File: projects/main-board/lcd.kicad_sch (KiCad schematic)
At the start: 10 parts

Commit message: Add footprints and 3D models
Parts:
- removed J1: ~, symbol symbol-library:NHD-4.3-480272EF-ASXP
- added J5: NHD-4.3-480272EF-ASXP (Molex 54104-4031), footprint-library:Molex 54104-4031, symbol symbol-library:NHD-4.3-480272EF-ASXP
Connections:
- net 3V3: now also J5.4 (VDD)
- net BACKLIGHT_N: now also J5.1 (LED-)
- net BACKLIGHT_P: now also J5.2 (LED+)
- net GND: now also J5.29 (GND), J5.3 (GND), J5.36 (GND)
- net LCD.B0: now also J5.21 (B0)
- net LCD.B1: now also J5.22 (B1)
- net LCD.B2: now also J5.23 (B2)
- net LCD.B3: now also J5.24 (B3)
- net LCD.B4: now also J5.25 (B4)
- net LCD.B5: now also J5.26 (B5)
- net LCD.B6: now also J5.27 (B6)
- net LCD.B7: now also J5.28 (B7)
- net LCD.CLK: now also J5.30 (CLKIN)
- net LCD.DE: now also J5.34 (DEN)
- net LCD.EN: now also J5.31 (STBYB)
- net LCD.G0: now also J5.13 (G0)
- net LCD.G1: now also J5.14 (G1)
- net LCD.G2: now also J5.15 (G2)
- net LCD.G3: now also J5.16 (G3)
- net LCD.G4: now also J5.17 (G4)
- net LCD.G5: now also J5.18 (G5)
- net LCD.G6: now also J5.19 (G6)
- net LCD.G7: now also J5.20 (G7)
- net LCD.HSYNC: now also J5.32 (HSD)
- net LCD.R0: now also J5.5 (R0)
- net LCD.R1: now also J5.6 (R1)
- net LCD.R2: now also J5.7 (R2)
- net LCD.R3: now also J5.8 (R3)
- net LCD.R4: now also J5.9 (R4)
- net LCD.R5: now also J5.10 (R5)
- net LCD.R6: now also J5.11 (R6)
- net LCD.R7: now also J5.12 (R7)
- net LCD.VSYNC: now also J5.33 (VSD)
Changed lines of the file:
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@@
-	)
-	(symbol
-		(lib_id "symbol-library:NHD-4.3-480272EF-ASXP")
-		(at 223.52 39.37 0)
-		(unit 1)
-		(exclude_from_sim no)
-		(in_bom yes)
-		(on_board yes)
-		(dnp no)
-		(property "Reference" "J1"
-			(at 224.536 38.1 0)
-			(effects
-				(font
-					(size 1.27 1.27)
-				)
-			)
-		)
-		(property "Value" "~"
-			(at 229.108 38.1 0)
-			(effects
-				(font
-					(size 1.27 1.27)
-				)
-			)
-		)
-		(property "Footprint" ""
-			(at 223.52 39.37 0)
-			(effects
-				(font
-					(size 1.27 1.27)
-				)
-				(hide yes)
-			)
-		)
-		(property "Datasheet" ""
-			(at 223.52 39.37 0)
-			(effects
-				(font
-					(size 1.27 1.27)
-				)
-				(hide yes)
-			)
-		)
-		(property "Description" ""
-			(at 223.52 39.37 0)
-			(effects
-				(font
-					(size 1.27 1.27)
-				)
-				(hide yes)
-			)
-		)
-		(pin "31"
-		)
-		(pin "2"
-		)
-		(pin "1"
-		)
-		(pin "29"
-		)
-		(pin "3"
-		)
-		(pin "36"
-		)
-		(pin "12"
-		)
-		(pin "13"
-		)
-		(pin "14"
-		)
-		(pin "15"
-		)
-		(pin "16"
-		)
-		(pin "17"
-		)
-		(pin "18"
-		)
-		(pin "19"
-		)
-		(pin "20"
-		)
-		(pin "21"
-		)
-		(pin "22"
-		)
-		(pin "23"
-		)
-		(pin "24"
-		)
-		(pin "25"
-		)
-		(pin "26"
-		)
-		(pin "27"
-		)
-		(pin "28"
-		)
-		(pin "35"
-		)
-		(pin "37"
-		)
-		(pin "38"
-		)
-		(pin "39"
-		)
-		(pin "40"
-		)
-		(pin "8"
-		)
-		(pin "9"
-		)
-		(pin "10"
-		)
-		(pin "11"
-		)
-		(pin "34"
-		)
-		(pin "33"
-		)
-		(pin "7"
-		)
-		(pin "4"
-		)
-		(pin "30"
-		)
-		(pin "5"
-		)
-		(pin "6"
-		)
-		(pin "32"
-		)
-		(instances
-			(project ""
-				(path "/c621b5fd-2ef7-4a67-960d-0ffc72b1245a/295cf080-cb0b-4f37-9a57-f3f4472bf120"
-					(reference "J1")
-					(unit 1)
-				)
-			)
-		)
 	)
 	(symbol
@@
 					(unit 1)
 				)
+			)
+		)
+	)
+	(symbol
+		(lib_name "NHD-4.3-480272EF-ASXP_1")
+		(lib_id "symbol-library:NHD-4.3-480272EF-ASXP")
+		(at 223.52 39.37 0)
+		(unit 1)
+		(exclude_from_sim no)
+		(in_bom yes)
+		(on_board yes)
+		(dnp no)
+		(fields_autoplaced yes)
+		(property "Reference" "J5"
+			(at 240.03 34.29 0)
+			(effects
+				(font
+					(size 1.27 1.27)
+				)
+			)
+		)
+		(property "Value" "NHD-4.3-480272EF-ASXP (Molex 54104-4031)"
+			(at 240.03 36.83 0)
+			(effects
+				(font
+					(size 1.27 1.27)
+				)
+			)
+		)
+		(property "Footprint" "footprint-library:Molex 54104-4031"
+			(at 237.49 148.59 0)
+			(effects
+				(font
+					(size 1.27 1.27)
+				)
+				(hide yes)
+			)
+		)
+		(property "Datasheet" ""
+			(at 223.52 39.37 0)
+			(effects
+				(font
+					(size 1.27 1.27)
+				)
+				(hide yes)
+			)
+		)
+		(property "Description" ""
+			(at 242.316 146.304 0)
+			(effects
+				(font
+					(size 1.27 1.27)
+				)
+				(hide yes)
+			)
+		)
+		(pin "5"
+		)
+		(pin "32"
+		)
+		(pin "13"
+		)
+		(pin "8"
+		)
+		(pin "16"
+		)
+		(pin "17"
+		)
+		(pin "18"
+		)
+		(pin "19"
+		)
+		(pin "20"
+		)
+		(pin "21"
+		)
+		(pin "22"
+		)
+		(pin "23"
+		)
+		(pin "24"
+		)
+		(pin "25"
+		)
+		(pin "26"
+		)
+		(pin "27"
+		)
+		(pin "28"
+		)
+		(pin "2"
+		)
+		(pin "1"
+		)
+		(pin "35"
+		)
+		(pin "37"
+		)
+		(pin "38"
+		)
+		(pin "39"
+		)
+		(pin "40"
+		)
+		(pin "29"
+		)
+		(pin "3"
+		)
+		(pin "36"
+		)
+		(pin "12"
+		)
+		(pin "34"
+		)
+		(pin "14"
+		)
+		(pin "15"
+		)
+		(pin "31"
+		)
+		(pin "9"
+		)
+		(pin "4"
+		)
+		(pin "7"
+		)
+		(pin "11"
+		)
+		(pin "10"
+		)
+		(pin "30"
+		)
+		(pin "33"
+		)
+		(pin "6"
+		)
+		(instances
+			(project "main-board"
+				(path "/c621b5fd-2ef7-4a67-960d-0ffc72b1245a/295cf080-cb0b-4f37-9a57-f3f4472bf120"
+					(reference "J5")
+					(unit 1)
+				)

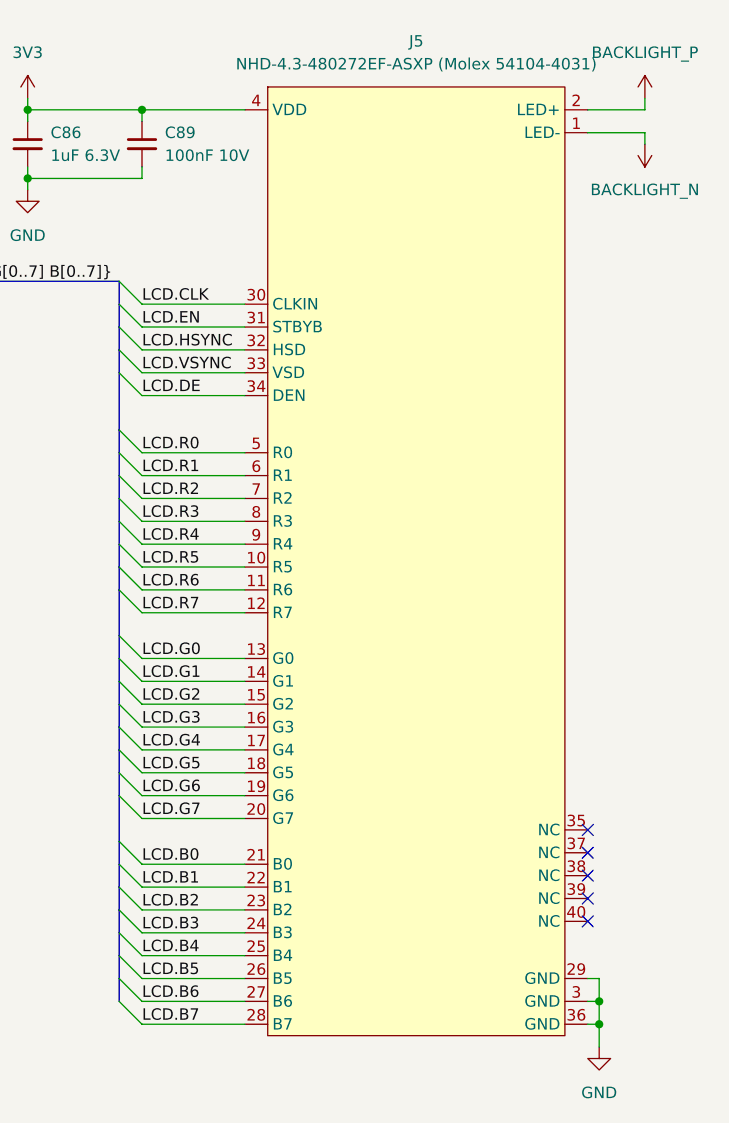
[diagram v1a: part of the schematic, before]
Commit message: Updated schematics with new symbols
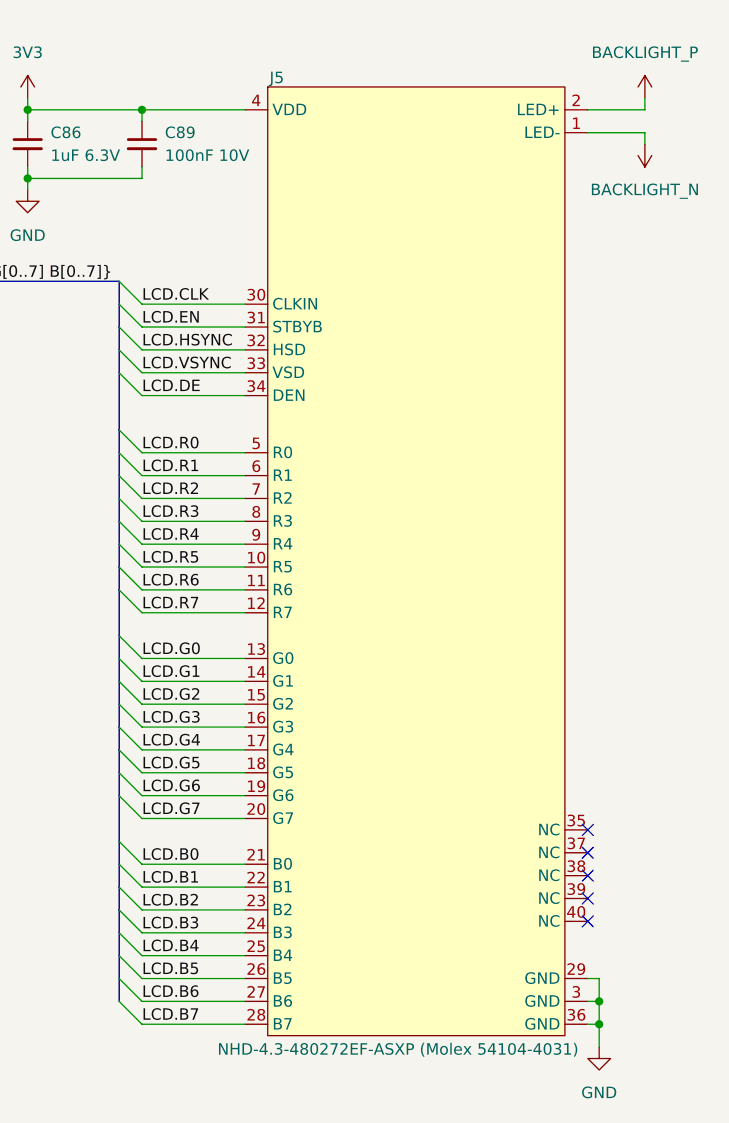
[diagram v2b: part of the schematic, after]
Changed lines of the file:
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@@
 		(on_board yes)
 		(dnp no)
-		(fields_autoplaced yes)
 		(property "Reference" "J5"
-			(at 240.03 34.29 0)
+			(at 224.536 38.354 0)
 			(effects
 				(font
@@
 		)
 		(property "Value" "NHD-4.3-480272EF-ASXP (Molex 54104-4031)"
-			(at 240.03 36.83 0)
+			(at 237.998 146.304 0)
 			(effects
 				(font

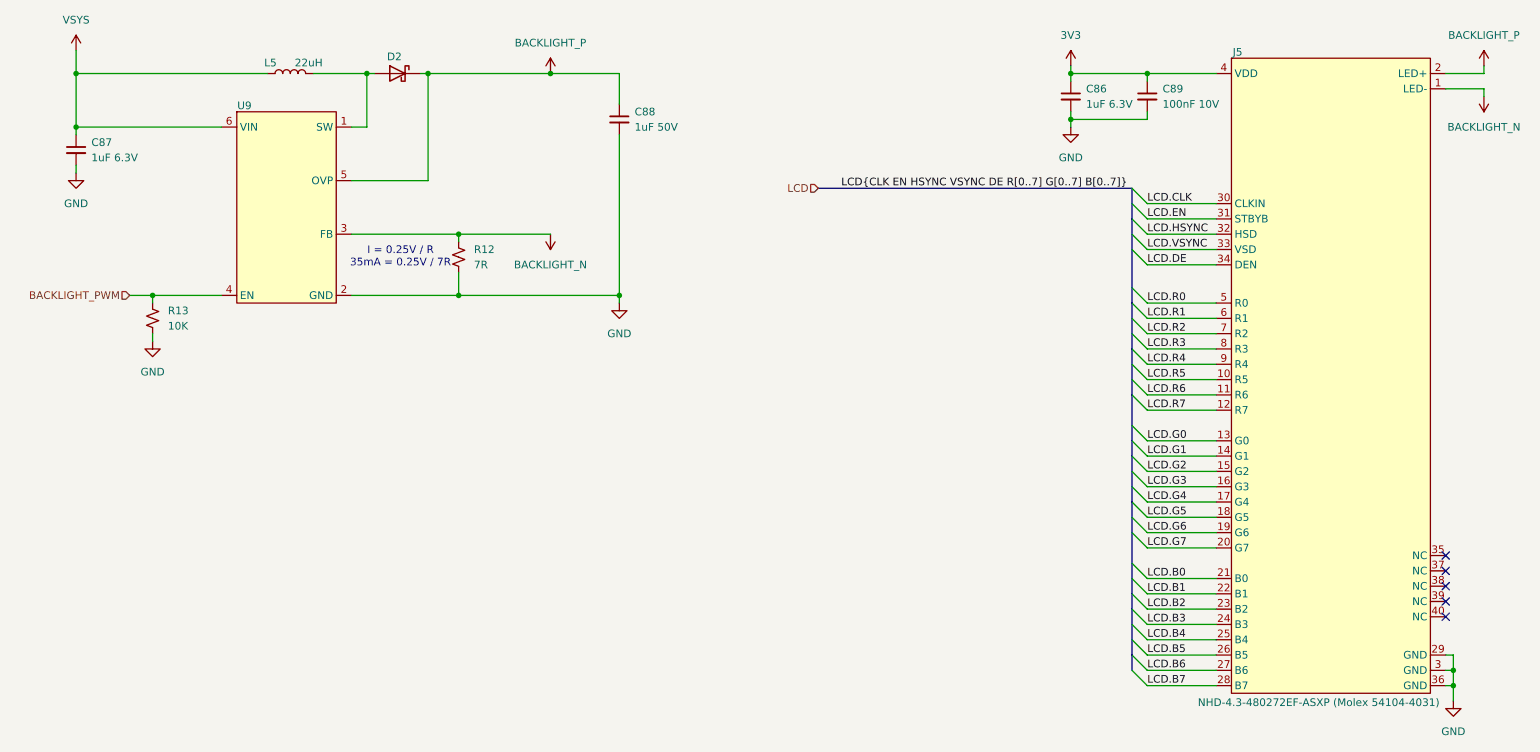
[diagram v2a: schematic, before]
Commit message: Re-annotate schematics.
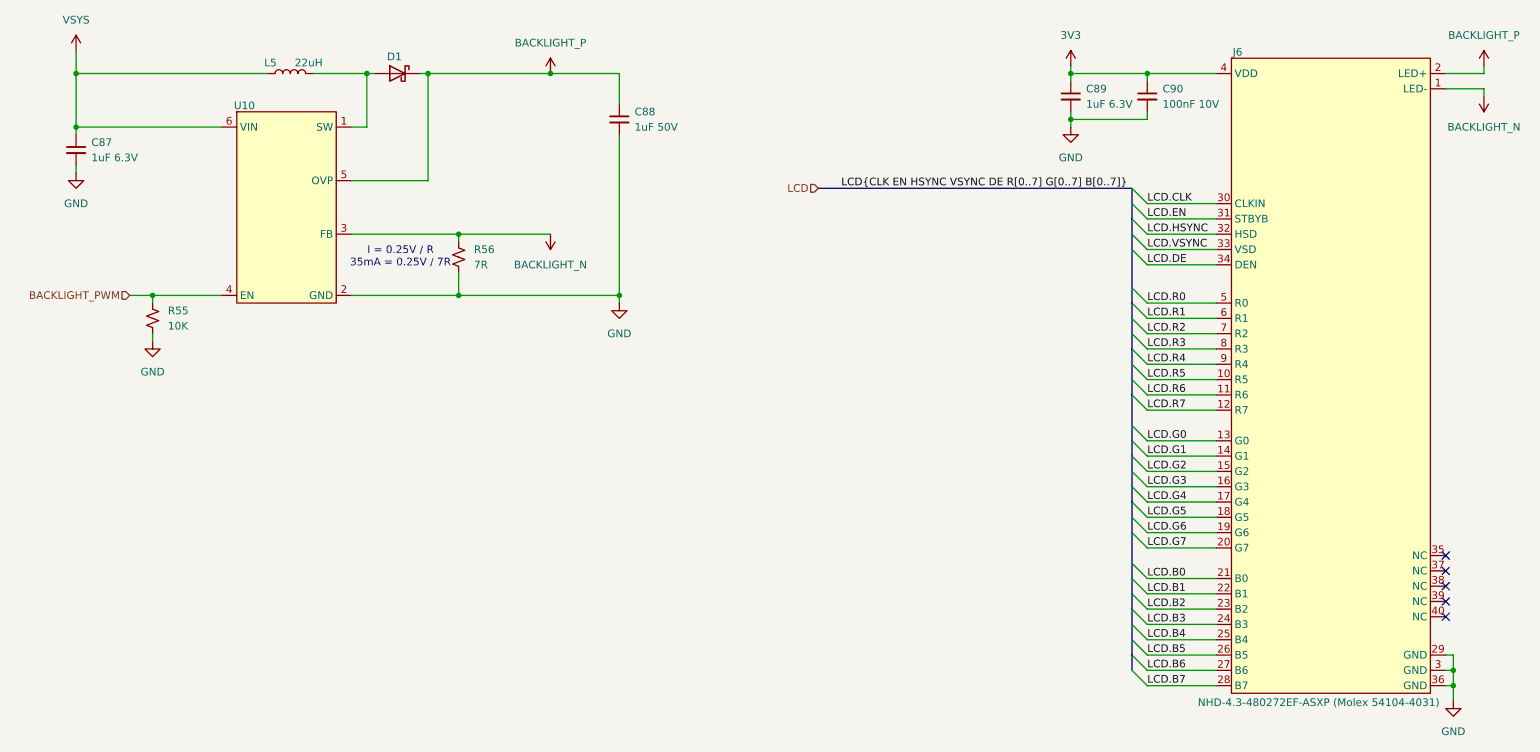
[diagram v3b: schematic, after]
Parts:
- renumbered C86 to C89, C89 to C90, D2 to D1, J5 to J6, R13 to R55, R12 to R56, U9 to U10
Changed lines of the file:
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@@
 		(on_board yes)
 		(dnp no)
-		(property "Reference" "D2"
+		(property "Reference" "D1"
 			(at 84.582 39.116 0)
 			(effects
@@
 			(project ""
 				(path "/c621b5fd-2ef7-4a67-960d-0ffc72b1245a/295cf080-cb0b-4f37-9a57-f3f4472bf120"
-					(reference "D2")
+					(reference "D1")
 					(unit 1)
 				)
@@
 		(dnp no)
 		(fields_autoplaced yes)
-		(property "Reference" "#PWR0115"
+		(property "Reference" "#PWR0130"
 			(at 121.92 86.36 0)
 			(effects
@@
 			(project "main-board"
 				(path "/c621b5fd-2ef7-4a67-960d-0ffc72b1245a/295cf080-cb0b-4f37-9a57-f3f4472bf120"
-					(reference "#PWR0115")
+					(reference "#PWR0130")
 					(unit 1)
 				)
@@
 		(dnp no)
 		(fields_autoplaced yes)
-		(property "Reference" "#PWR0113"
+		(property "Reference" "#PWR0129"
 			(at 110.49 64.77 0)
 			(effects
@@
 			(project "main-board"
 				(path "/c621b5fd-2ef7-4a67-960d-0ffc72b1245a/295cf080-cb0b-4f37-9a57-f3f4472bf120"
-					(reference "#PWR0113")
+					(reference "#PWR0129")
 					(unit 1)
 				)
@@
 		(dnp no)
 		(fields_autoplaced yes)
-		(property "Reference" "R12"
+		(property "Reference" "R56"
 			(at 97.79 71.1199 0)
 			(effects
@@
 			(project "main-board"
 				(path "/c621b5fd-2ef7-4a67-960d-0ffc72b1245a/295cf080-cb0b-4f37-9a57-f3f4472bf120"
-					(reference "R12")
+					(reference "R56")
 					(unit 1)
 				)
@@
 		(on_board yes)
 		(dnp no)
-		(property "Reference" "U9"
+		(property "Reference" "U10"
 			(at 59.69 47.244 0)
 			(effects
@@
 			(project ""
 				(path "/c621b5fd-2ef7-4a67-960d-0ffc72b1245a/295cf080-cb0b-4f37-9a57-f3f4472bf120"
-					(reference "U9")
+					(reference "U10")
 					(unit 1)
 				)
@@
 		(dnp no)
 		(fields_autoplaced yes)
-		(property "Reference" "#PWR0114"
+		(property "Reference" "#PWR0126"
 			(at 31.75 64.77 0)
 			(effects
@@
 			(project "main-board"
 				(path "/c621b5fd-2ef7-4a67-960d-0ffc72b1245a/295cf080-cb0b-4f37-9a57-f3f4472bf120"
-					(reference "#PWR0114")
+					(reference "#PWR0126")
 					(unit 1)
 				)
@@
 		(dnp no)
 		(fields_autoplaced yes)
-		(property "Reference" "#PWR0119"
+		(property "Reference" "#PWR0135"
 			(at 265.43 41.91 0)
 			(effects
@@
 			(project "main-board"
 				(path "/c621b5fd-2ef7-4a67-960d-0ffc72b1245a/295cf080-cb0b-4f37-9a57-f3f4472bf120"
-					(reference "#PWR0119")
+					(reference "#PWR0135")
 					(unit 1)
 				)
@@
 		(dnp no)
 		(fields_autoplaced yes)
-		(property "Reference" "#PWR0109"
+		(property "Reference" "#PWR0133"
 			(at 260.35 152.4 0)
 			(effects
@@
 			(project ""
 				(path "/c621b5fd-2ef7-4a67-960d-0ffc72b1245a/295cf080-cb0b-4f37-9a57-f3f4472bf120"
-					(reference "#PWR0109")
+					(reference "#PWR0133")
 					(unit 1)
 				)
@@
 		(dnp no)
 		(fields_autoplaced yes)
-		(property "Reference" "#PWR0112"
+		(property "Reference" "#PWR0131"
 			(at 196.85 44.45 0)
 			(effects
@@
 			(project "main-board"
 				(path "/c621b5fd-2ef7-4a67-960d-0ffc72b1245a/295cf080-cb0b-4f37-9a57-f3f4472bf120"
-					(reference "#PWR0112")
+					(reference "#PWR0131")
 					(unit 1)
 				)
@@
 		(dnp no)
 		(fields_autoplaced yes)
-		(property "Reference" "C89"
+		(property "Reference" "C90"
 			(at 212.09 44.4562 0)
 			(effects
@@
 			(project "main-board"
 				(path "/c621b5fd-2ef7-4a67-960d-0ffc72b1245a/295cf080-cb0b-4f37-9a57-f3f4472bf120"
-					(reference "C89")
+					(reference "C90")
 					(unit 1)
 				)
@@
 		(dnp no)
 		(fields_autoplaced yes)
-		(property "Reference" "#PWR0117"
+		(property "Reference" "#PWR0132"
 			(at 196.85 57.15 0)
 			(effects
@@
 			(project "main-board"
 				(path "/c621b5fd-2ef7-4a67-960d-0ffc72b1245a/295cf080-cb0b-4f37-9a57-f3f4472bf120"
-					(reference "#PWR0117")
+					(reference "#PWR0132")
 					(unit 1)
 				)
@@
 		(dnp no)
 		(fields_autoplaced yes)
-		(property "Reference" "#PWR0116"
+		(property "Reference" "#PWR0128"
 			(at 110.49 45.72 0)
 			(effects
@@
 			(project "main-board"
 				(path "/c621b5fd-2ef7-4a67-960d-0ffc72b1245a/295cf080-cb0b-4f37-9a57-f3f4472bf120"
-					(reference "#PWR0116")
+					(reference "#PWR0128")
 					(unit 1)
 				)
@@
 		(dnp no)
 		(fields_autoplaced yes)
-		(property "Reference" "#PWR0118"
+		(property "Reference" "#PWR0134"
 			(at 265.43 44.45 0)
 			(effects
@@
 			(project "main-board"
 				(path "/c621b5fd-2ef7-4a67-960d-0ffc72b1245a/295cf080-cb0b-4f37-9a57-f3f4472bf120"
-					(reference "#PWR0118")
+					(reference "#PWR0134")
 					(unit 1)
 				)
@@
 		(on_board yes)
 		(dnp no)
-		(property "Reference" "J5"
+		(property "Reference" "J6"
 			(at 224.536 38.354 0)
 			(effects
@@
 			(project "main-board"
 				(path "/c621b5fd-2ef7-4a67-960d-0ffc72b1245a/295cf080-cb0b-4f37-9a57-f3f4472bf120"
-					(reference "J5")
+					(reference "J6")
 					(unit 1)
 				)
@@
 		(dnp no)
 		(fields_autoplaced yes)
-		(property "Reference" "#PWR0110"
+		(property "Reference" "#PWR0127"
 			(at 44.45 92.71 0)
 			(effects
@@
 			(project "main-board"
 				(path "/c621b5fd-2ef7-4a67-960d-0ffc72b1245a/295cf080-cb0b-4f37-9a57-f3f4472bf120"
-					(reference "#PWR0110")
+					(reference "#PWR0127")
 					(unit 1)
 				)
@@
 		(dnp no)
 		(fields_autoplaced yes)
-		(property "Reference" "#PWR0111"
+		(property "Reference" "#PWR0125"
 			(at 31.75 41.91 0)
 			(effects
@@
 			(project ""
 				(path "/c621b5fd-2ef7-4a67-960d-0ffc72b1245a/295cf080-cb0b-4f37-9a57-f3f4472bf120"
-					(reference "#PWR0111")
+					(reference "#PWR0125")
 					(unit 1)
 				)
@@
 		(dnp no)
 		(fields_autoplaced yes)
-		(property "Reference" "R13"
+		(property "Reference" "R55"
 			(at 46.99 81.2799 0)
 			(effects
@@
 			(project "main-board"
 				(path "/c621b5fd-2ef7-4a67-960d-0ffc72b1245a/295cf080-cb0b-4f37-9a57-f3f4472bf120"
-					(reference "R13")
+					(reference "R55")
 					(unit 1)
 				)
@@
 		(dnp no)
 		(fields_autoplaced yes)
-		(property "Reference" "C86"
+		(property "Reference" "C89"
 			(at 199.39 44.4562 0)
 			(effects
@@
 			(project "main-board"
 				(path "/c621b5fd-2ef7-4a67-960d-0ffc72b1245a/295cf080-cb0b-4f37-9a57-f3f4472bf120"
-					(reference "C86")
-					(unit 1)
-				)
+					(reference "C89")
+					(unit 1)
+				)

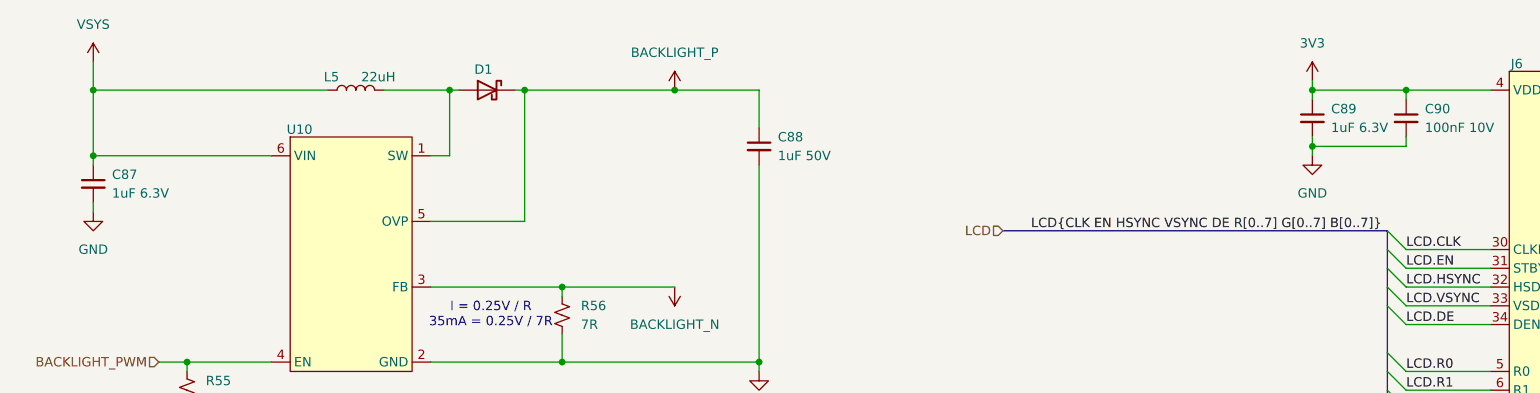
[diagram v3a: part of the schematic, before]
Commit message: Add capacitor part library.
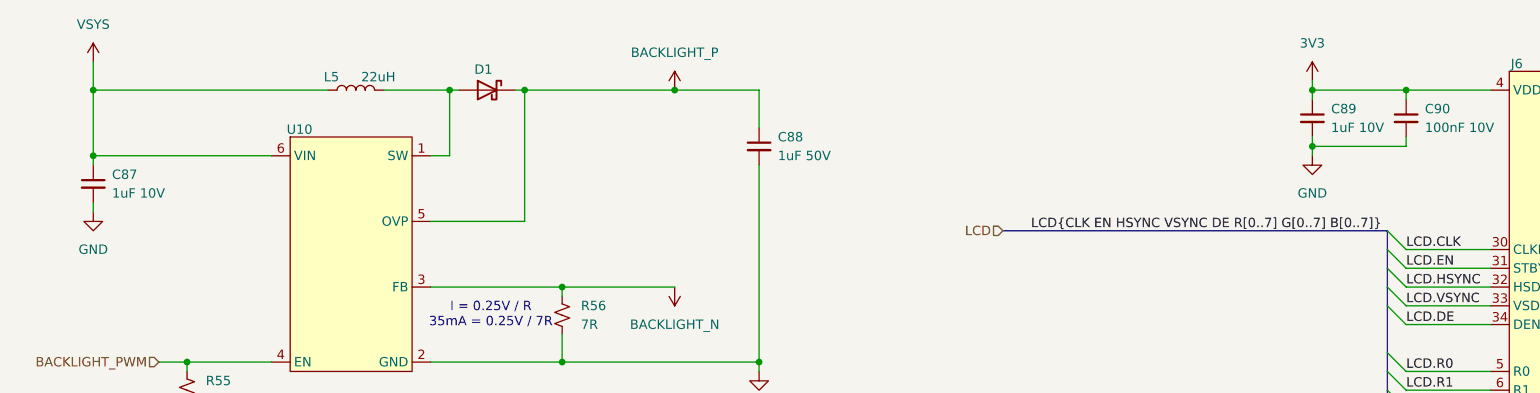
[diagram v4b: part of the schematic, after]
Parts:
- C87, C89: value 1uF 6.3V -> 1uF 10V
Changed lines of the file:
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@@
 			)
 		)
-		(property "Value" "1uF 6.3V"
+		(property "Value" "1uF 10V"
 			(at 199.39 46.9962 0)
 			(effects
@@
 			)
 		)
-		(property "Value" "1uF 6.3V"
+		(property "Value" "1uF 10V"
 			(at 34.29 55.8862 0)
 			(effects
